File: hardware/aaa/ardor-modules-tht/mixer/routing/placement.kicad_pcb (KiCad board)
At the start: 2 copper layers, 100 x 75 mm, 30 parts, among them J101 5V POWER INPUT, J102 STEREO AUDIO INPUT FROM SOURCE, J103 BUFFERED STEREO + MONO AUDIO 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, U401 MCP6022-I/P, U402 MCP6022-I/P

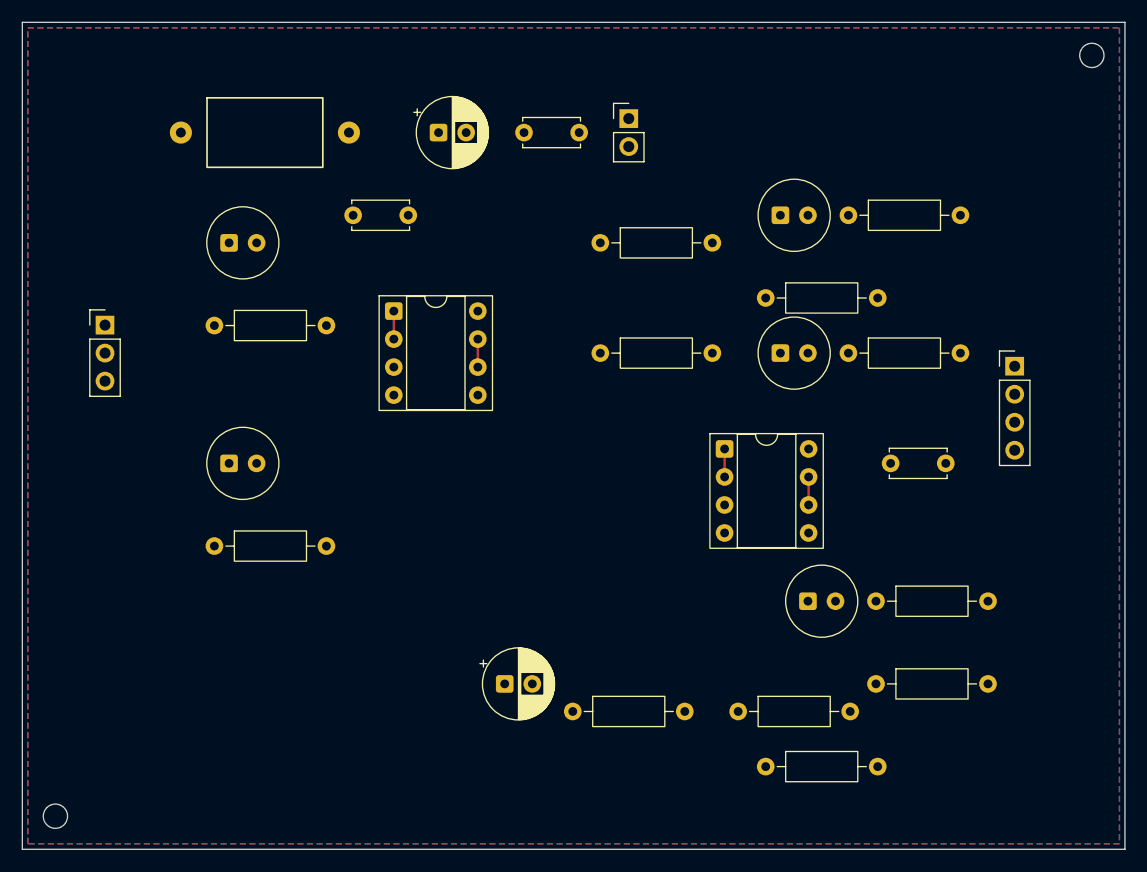
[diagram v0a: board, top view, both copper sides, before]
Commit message: feat(hardware): compact layouts and adopt Hestore module packages
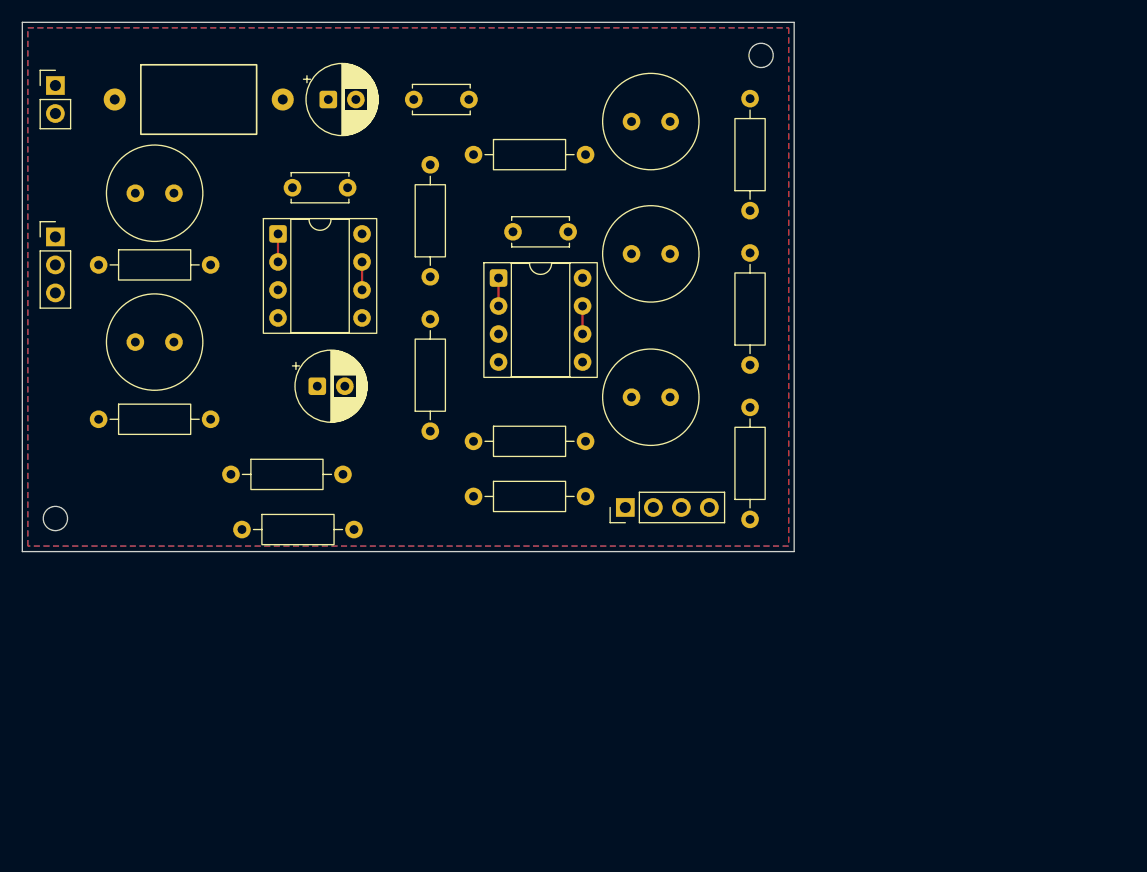
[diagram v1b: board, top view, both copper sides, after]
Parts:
- C401, C402, C407, C408, C409: value 10u / 25V BIPOLAR -> 10u / 50V BIPOLAR; footprint Ardor_THT:CP_Bipolar_D6.3mm_P2.50mm -> Ardor_THT:CP_Bipolar_Nichicon_D8.0mm_P3.50mm
- moved J101 52.1 mm to (53.0, 55.7)
- moved R406 47.9 mm to (69.9, 96.0)
- moved C405 40.2 mm to (94.5, 69.0)
- moved R411 39.3 mm to (90.9, 88.0)
- moved R405 37.7 mm to (68.9, 91.0)
- moved J103 37.6 mm to (104.7, 94.0), turned to 90 degrees
- moved R412 36.1 mm to (90.9, 93.0)
- moved C403 31.9 mm to (76.8, 83.0)
- moved H2 30.0 mm to (117.0, 53.0)
- moved R410 29.5 mm to (90.9, 62.0)
- moved H1 27.0 mm to (53.0, 95.0)
- moved U402 25.7 mm to (93.2, 73.2)
- moved C409 24.5 mm to (105.2, 84.0)
- moved R409 18.8 mm to (116.0, 95.1), turned to 90 degrees
- moved R404 17.0 mm to (87.0, 87.1), turned to 90 degrees
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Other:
- board size 100 x 75 mm -> 70 x 48 mm
